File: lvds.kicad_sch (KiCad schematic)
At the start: 20 parts, among them J1 Conn_01x22_Female, J3 Conn_01x34_Female, J5 Conn_01x02_Female, U1 SN65DSI83TPAPRQ1

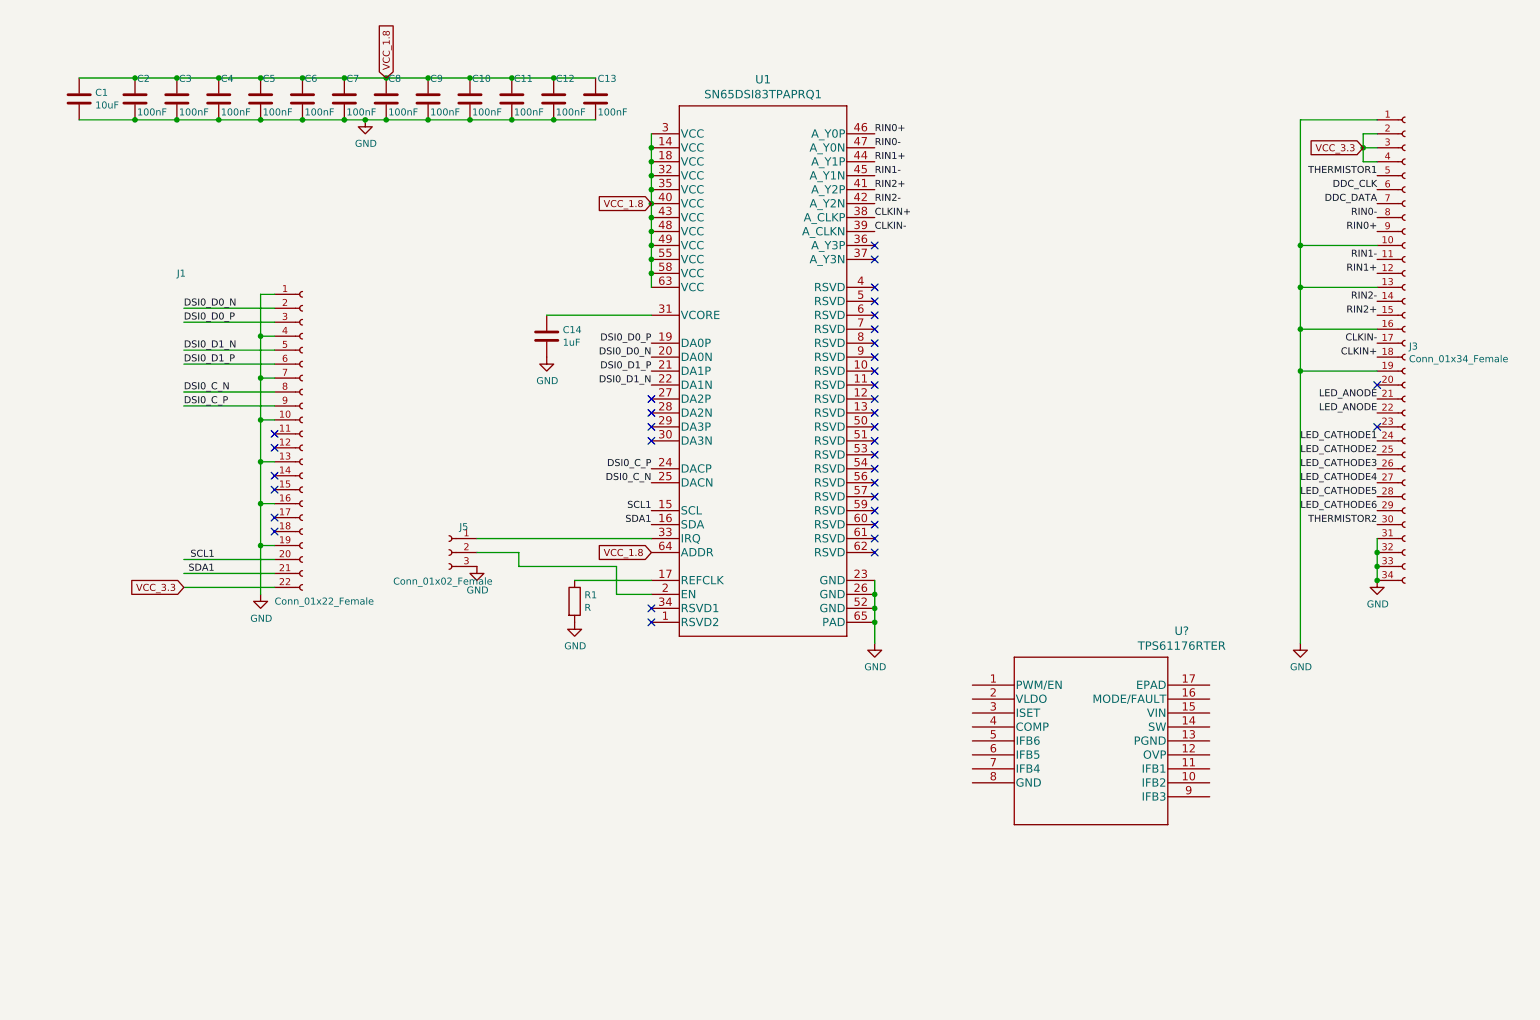
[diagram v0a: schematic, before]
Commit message: LED driver: Set max voltage to 12V with 1M/143K divider on OVP pin; set full-scale current to 20mA with 53.6K resistor on ISET. Choose dimming mode 1 with 1.3M resistor to ground on mode/fault.
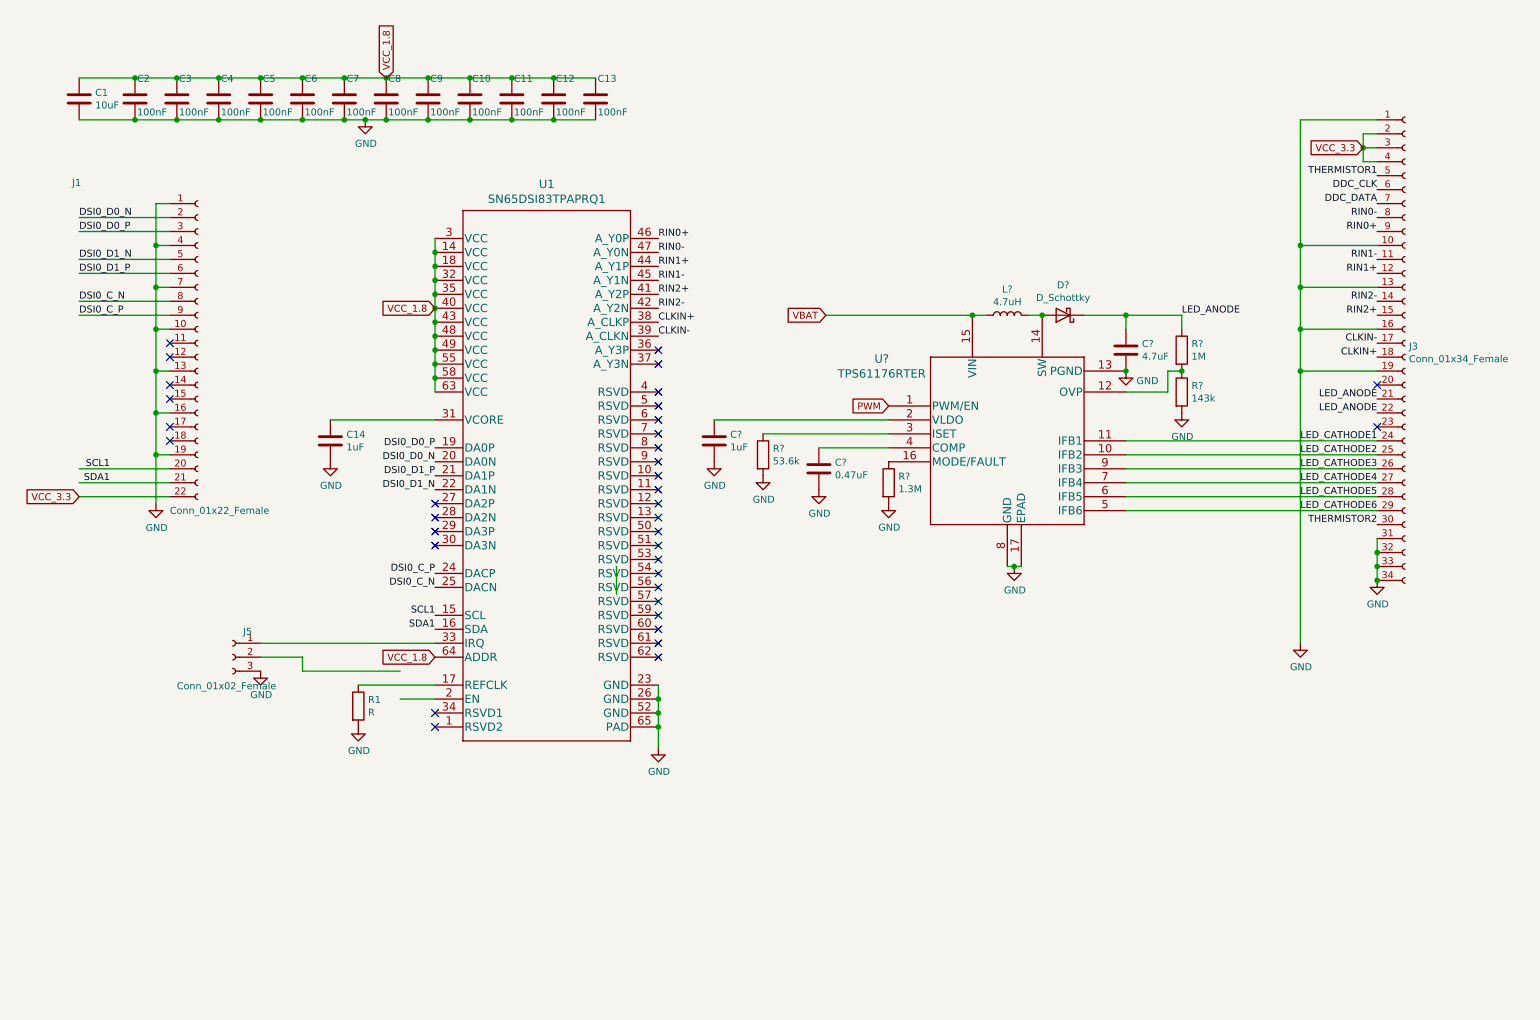
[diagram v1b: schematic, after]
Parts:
- added C?: 4.7uF, symbol Device:C
- added C?: 1uF, symbol Device:C
- added C?: 0.47uF, symbol Device:C
- added D?: D_Schottky, symbol Device:D_Schottky
- added L?: 4.7uH, symbol Device:L
- added R?: 143k, symbol Device:R
- added R?: 1.3M, symbol Device:R
- added R?: 53.6k, symbol Device:R
- added R?: 1M, symbol Device:R
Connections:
- net GND: now also U?.13 (PGND), U?.17 (EPAD), U?.8 (GND), C?.2, C?.2, C?.2, R?.2, R?.2, R?.2
- net LED_ANODE: now also C?.1, D?.1 (K), R?.1
- net LED_CATHODE1: now also U?.11 (IFB1)
- net LED_CATHODE2: now also U?.10 (IFB2)
- net LED_CATHODE3: now also U?.9 (IFB3)
- net LED_CATHODE4: now also U?.7 (IFB4)
- net LED_CATHODE5: now also U?.6 (IFB5)
- net LED_CATHODE6: now also U?.5 (IFB6)
- net PWM: now reaches U?.1 (PWM/EN)
- net at U?.12 (OVP): now also R?.1, R?.2
- net at U?.14 (SW): now also D?.2 (A), L?.2
- net VBAT: now reaches U?.15 (VIN)
- net VBAT: now also L?.1
- net at U?.16 (MODE/FAULT): now also R?.1
- net at U?.2 (VLDO): now also C?.1
- net at U?.3 (ISET): now also R?.1
- net at U?.4 (COMP): now also C?.1
- net at J5.2 (Pin_2): no longer U1.2 (EN)
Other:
- moved on the sheet: C14, J1, J5, R1, U1, U?

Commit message: Fix ERC errors
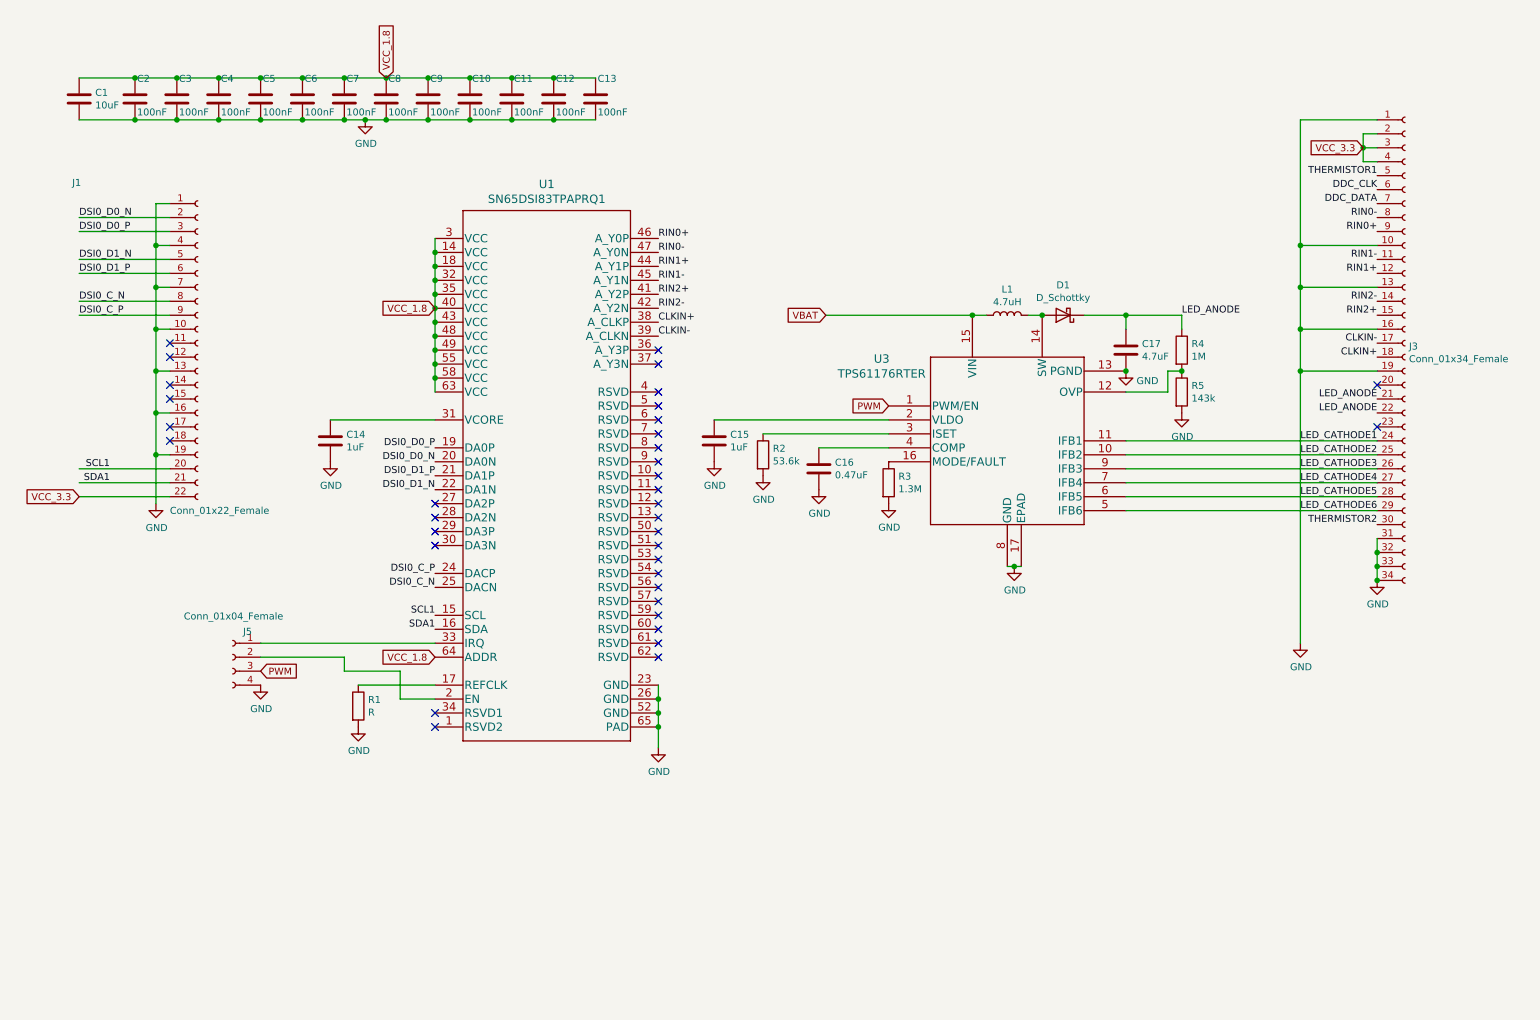
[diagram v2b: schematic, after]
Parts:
- J5: value Conn_01x02_Female -> Conn_01x04_Female; symbol Connector:Conn_01x03_Female -> Connector:Conn_01x04_Female
- gave numbers to parts that had none: 10
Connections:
- net GND: now also J5.4 (Pin_4); no longer J5.3 (Pin_3)
- net PWM: now also J5.3 (Pin_3)
- net at J5.2 (Pin_2): now also U1.2 (EN)
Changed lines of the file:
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@@
-    (stroke (width 0) (type solid) (color 0 0 0 0))
-  )
-  (wire (pts (xy 66.04 127) (xy 58.42 127))
-    (stroke (width 0) (type solid) (color 0 0 0 0))
-  )
-  (wire (pts (xy 66.04 129.54) (xy 66.04 127))
     (stroke (width 0) (type solid) (color 0 0 0 0))
   )
@@
     (stroke (width 0) (type solid) (color 0 0 0 0))
   )
+  (wire (pts (xy 73.66 127) (xy 58.42 127))
+    (stroke (width 0) (type solid) (color 0 0 0 0))
+  )
+  (wire (pts (xy 73.66 129.54) (xy 73.66 127))
+    (stroke (width 0) (type solid) (color 0 0 0 0))
+  )
   (wire (pts (xy 76.2 132.08) (xy 90.17 132.08))
     (stroke (width 0) (type solid) (color 0 0 0 0))
@@
     (stroke (width 0) (type solid) (color 0 0 0 0))
   )
-  (wire (pts (xy 83.82 129.54) (xy 66.04 129.54))
+  (wire (pts (xy 83.82 129.54) (xy 73.66 129.54))
+    (stroke (width 0) (type solid) (color 0 0 0 0))
+  )
+  (wire (pts (xy 83.82 129.54) (xy 83.82 134.62))
     (stroke (width 0) (type solid) (color 0 0 0 0))
   )
@@
   )
   (wire (pts (xy 111.76 29.21) (xy 119.38 29.21))
-    (stroke (width 0) (type solid) (color 0 0 0 0))
-  )
-  (wire (pts (xy 123.19 115.57) (xy 123.19 110.49))
     (stroke (width 0) (type solid) (color 0 0 0 0))
   )
@@
     )
   )
+  (global_label "PWM" (shape input) (at 58.42 129.54 0)
+    (effects (font (size 1.27 1.27)) (justify left))
+    (property "Intersheet References" "${INTERSHEET_REFS}" (id 0) (at 65.006 129.6194 0)
+      (effects (font (size 1.27 1.27)) (justify left) hide)
+    )
+  )
   (global_label "VCC_1.8" (shape input) (at 81.28 21.59 90)
     (effects (font (size 1.27 1.27)) (justify left))
@@
   (symbol (lib_id "Device:L") (at 194.31 64.77 90) (unit 1)
     (in_bom yes) (on_board yes)
-    (property "Reference" "L?" (id 0) (at 194.31 60.0518 90))
+    (property "Reference" "L1" (id 0) (at 194.31 60.0518 90))
     (property "Value" "4.7uH" (id 1) (at 194.31 62.35 90))
     (property "Footprint" "" (id 2) (at 194.31 64.77 0)
@@
     (pin "1")
   )
-  (symbol (lib_id "power:GND") (at 58.42 129.54 0) (unit 1)
-    (in_bom yes) (on_board yes)
-    (property "Reference" "#PWR0108" (id 0) (at 58.42 135.89 0)
-      (effects (font (size 1.27 1.27)) hide)
-    )
-    (property "Value" "GND" (id 1) (at 58.5343 133.8644 0))
-    (property "Footprint" "" (id 2) (at 58.42 129.54 0)
-      (effects (font (size 1.27 1.27)) hide)
-    )
-    (property "Datasheet" "" (id 3) (at 58.42 129.54 0)
+  (symbol (lib_id "power:GND") (at 58.42 132.08 0) (unit 1)
+    (in_bom yes) (on_board yes)
+    (property "Reference" "#PWR0108" (id 0) (at 58.42 138.43 0)
+      (effects (font (size 1.27 1.27)) hide)
+    )
+    (property "Value" "GND" (id 1) (at 58.5343 136.4044 0))
+    (property "Footprint" "" (id 2) (at 58.42 132.08 0)
+      (effects (font (size 1.27 1.27)) hide)
+    )
+    (property "Datasheet" "" (id 3) (at 58.42 132.08 0)
       (effects (font (size 1.27 1.27)) hide)
     )
@@
   (symbol (lib_id "power:GND") (at 140.97 91.44 0) (unit 1)
     (in_bom yes) (on_board yes)
-    (property "Reference" "#PWR?" (id 0) (at 140.97 97.79 0)
+    (property "Reference" "#PWR03" (id 0) (at 140.97 97.79 0)
       (effects (font (size 1.27 1.27)) hide)
     )
@@
   (symbol (lib_id "power:GND") (at 149.86 93.98 0) (unit 1)
     (in_bom yes) (on_board yes)
-    (property "Reference" "#PWR?" (id 0) (at 149.86 100.33 0)
+    (property "Reference" "#PWR04" (id 0) (at 149.86 100.33 0)
       (effects (font (size 1.27 1.27)) hide)
     )
@@
   (symbol (lib_id "power:GND") (at 160.02 96.52 0) (unit 1)
     (in_bom yes) (on_board yes)
-    (property "Reference" "#PWR?" (id 0) (at 160.02 102.87 0)
+    (property "Reference" "#PWR05" (id 0) (at 160.02 102.87 0)
       (effects (font (size 1.27 1.27)) hide)
     )
@@
   (symbol (lib_id "power:GND") (at 172.72 99.06 0) (unit 1)
     (in_bom yes) (on_board yes)
-    (property "Reference" "#PWR?" (id 0) (at 172.72 105.41 0)
+    (property "Reference" "#PWR06" (id 0) (at 172.72 105.41 0)
       (effects (font (size 1.27 1.27)) hide)
     )
@@
   (symbol (lib_id "power:GND") (at 195.58 110.49 0) (unit 1)
     (in_bom yes) (on_board yes)
-    (property "Reference" "#PWR?" (id 0) (at 195.58 116.84 0)
+    (property "Reference" "#PWR07" (id 0) (at 195.58 116.84 0)
       (effects (font (size 1.27 1.27)) hide)
     )
@@
   (symbol (lib_id "power:GND") (at 215.9 74.93 0) (unit 1)
     (in_bom yes) (on_board yes)
-    (property "Reference" "#PWR?" (id 0) (at 215.9 81.28 0)
+    (property "Reference" "#PWR08" (id 0) (at 215.9 81.28 0)
       (effects (font (size 1.27 1.27)) hide)
     )
@@
   (symbol (lib_id "power:GND") (at 226.06 82.55 0) (unit 1)
     (in_bom yes) (on_board yes)
-    (property "Reference" "#PWR?" (id 0) (at 226.06 88.9 0)
+    (property "Reference" "#PWR09" (id 0) (at 226.06 88.9 0)
       (effects (font (size 1.27 1.27)) hide)
     )
@@
   (symbol (lib_id "Device:R") (at 149.86 90.17 0) (unit 1)
     (in_bom yes) (on_board yes)
-    (property "Reference" "R?" (id 0) (at 151.6381 89.0206 0)
+    (property "Reference" "R2" (id 0) (at 151.6381 89.0206 0)
       (effects (font (size 1.27 1.27)) (justify left))
     )
@@
   (symbol (lib_id "Device:R") (at 172.72 95.25 0) (unit 1)
     (in_bom yes) (on_board yes)
-    (property "Reference" "R?" (id 0) (at 174.4981 94.1006 0)
+    (property "Reference" "R3" (id 0) (at 174.4981 94.1006 0)
       (effects (font (size 1.27 1.27)) (justify left))
     )
@@
   (symbol (lib_id "Device:R") (at 226.06 71.12 0) (unit 1)
     (in_bom yes) (on_board yes)
-    (property "Reference" "R?" (id 0) (at 227.8381 69.9706 0)
+    (property "Reference" "R4" (id 0) (at 227.8381 69.9706 0)
       (effects (font (size 1.27 1.27)) (justify left))
     )
@@
   (symbol (lib_id "Device:R") (at 226.06 78.74 0) (unit 1)
     (in_bom yes) (on_board yes)
-    (property "Reference" "R?" (id 0) (at 227.8381 77.5906 0)
+    (property "Reference" "R5" (id 0) (at 227.8381 77.5906 0)
       (effects (font (size 1.27 1.27)) (justify left))
     )
@@
   (symbol (lib_id "Device:D_Schottky") (at 204.47 64.77 180) (unit 1)
     (in_bom yes) (on_board yes)
-    (property "Reference" "D?" (id 0) (at 204.47 59.2898 0))
+    (property "Reference" "D1" (id 0) (at 204.47 59.2898 0))
     (property "Value" "D_Schottky" (id 1) (at 204.47 61.5885 0))
     (property "Footprint" "" (id 2) (at 204.47 64.77 0)
@@
   (symbol (lib_id "Device:C") (at 140.97 87.63 0) (unit 1)
     (in_bom yes) (on_board yes)
-    (property "Reference" "C?" (id 0) (at 143.8911 86.4806 0)
+    (property "Reference" "C15" (id 0) (at 143.8911 86.4806 0)
       (effects (font (size 1.27 1.27)) (justify left))
     )
@@
   (symbol (lib_id "Device:C") (at 160.02 92.71 0) (unit 1)
     (in_bom yes) (on_board yes)
-    (property "Reference" "C?" (id 0) (at 162.9411 91.5606 0)
+    (property "Reference" "C16" (id 0) (at 162.9411 91.5606 0)
       (effects (font (size 1.27 1.27)) (justify left))
     )
@@
   (symbol (lib_id "Device:C") (at 215.9 71.12 0) (unit 1)
     (in_bom yes) (on_board yes)
-    (property "Reference" "C?" (id 0) (at 218.8211 69.9706 0)
+    (property "Reference" "C17" (id 0) (at 218.8211 69.9706 0)
       (effects (font (size 1.27 1.27)) (justify left))
     )
@@
     (pin "2")
   )
-  (symbol (lib_id "Connector:Conn_01x03_Female") (at 53.34 127 0) (mirror y) (unit 1)
+  (symbol (lib_id "Connector:Conn_01x04_Female") (at 53.34 127 0) (mirror y) (unit 1)
     (in_bom yes) (on_board yes)
     (property "Reference" "J5" (id 0) (at 56.0324 122.3326 0))
-    (property "Value" "Conn_01x02_Female" (id 1) (at 52.2224 132.2513 0))
+    (property "Value" "Conn_01x04_Female" (id 1) (at 53.492 119.551 0))
     (property "Footprint" "" (id 2) (at 53.34 127 0)
       (effects (font (size 1.27 1.27)) hide)
@@
     (pin "2")
     (pin "3")
+    (pin "4")
   )
   (symbol (lib_id "Connector:Conn_01x22_Female") (at 46.99 69.85 0) (unit 1)
@@
   (symbol (lib_id "TPS61176RTER:TPS61176RTER") (at 172.72 77.47 0) (unit 1)
     (in_bom yes) (on_board yes)
-    (property "Reference" "U?" (id 0) (at 171.45 72.71 0)
+    (property "Reference" "U3" (id 0) (at 171.45 72.71 0)
       (effects (font (size 1.524 1.524)))
     )
